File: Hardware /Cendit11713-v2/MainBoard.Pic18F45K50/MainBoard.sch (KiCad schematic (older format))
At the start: 32 parts, among them CON1 VIKING_BOARD_CON, CON2 USB_CON, J1 RESET_CON, U1 PIC18F45K50-X/PT, U2 SER_BUS_ADDR_CON

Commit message: Respaldo rapido
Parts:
- CON2: symbol USB_CON -> USB_CON-RESCUE-MainBoard
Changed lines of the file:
@@
 EESchema Schematic File Version 2
+LIBS:MainBoard-rescue
 LIBS:adc-dac
 LIBS:memory
@@
 $EndComp
 $Comp
-L POWER_CON #CON01
+L POWER_CON-RESCUE-MainBoard #CON01
 U 1 1 5996E2AE
 P 1000 2000
@@
 $EndComp
 $Comp
-L USB_CON CON2
+L USB_CON-RESCUE-MainBoard CON2
 U 1 1 5996E56B
 P 1000 3000

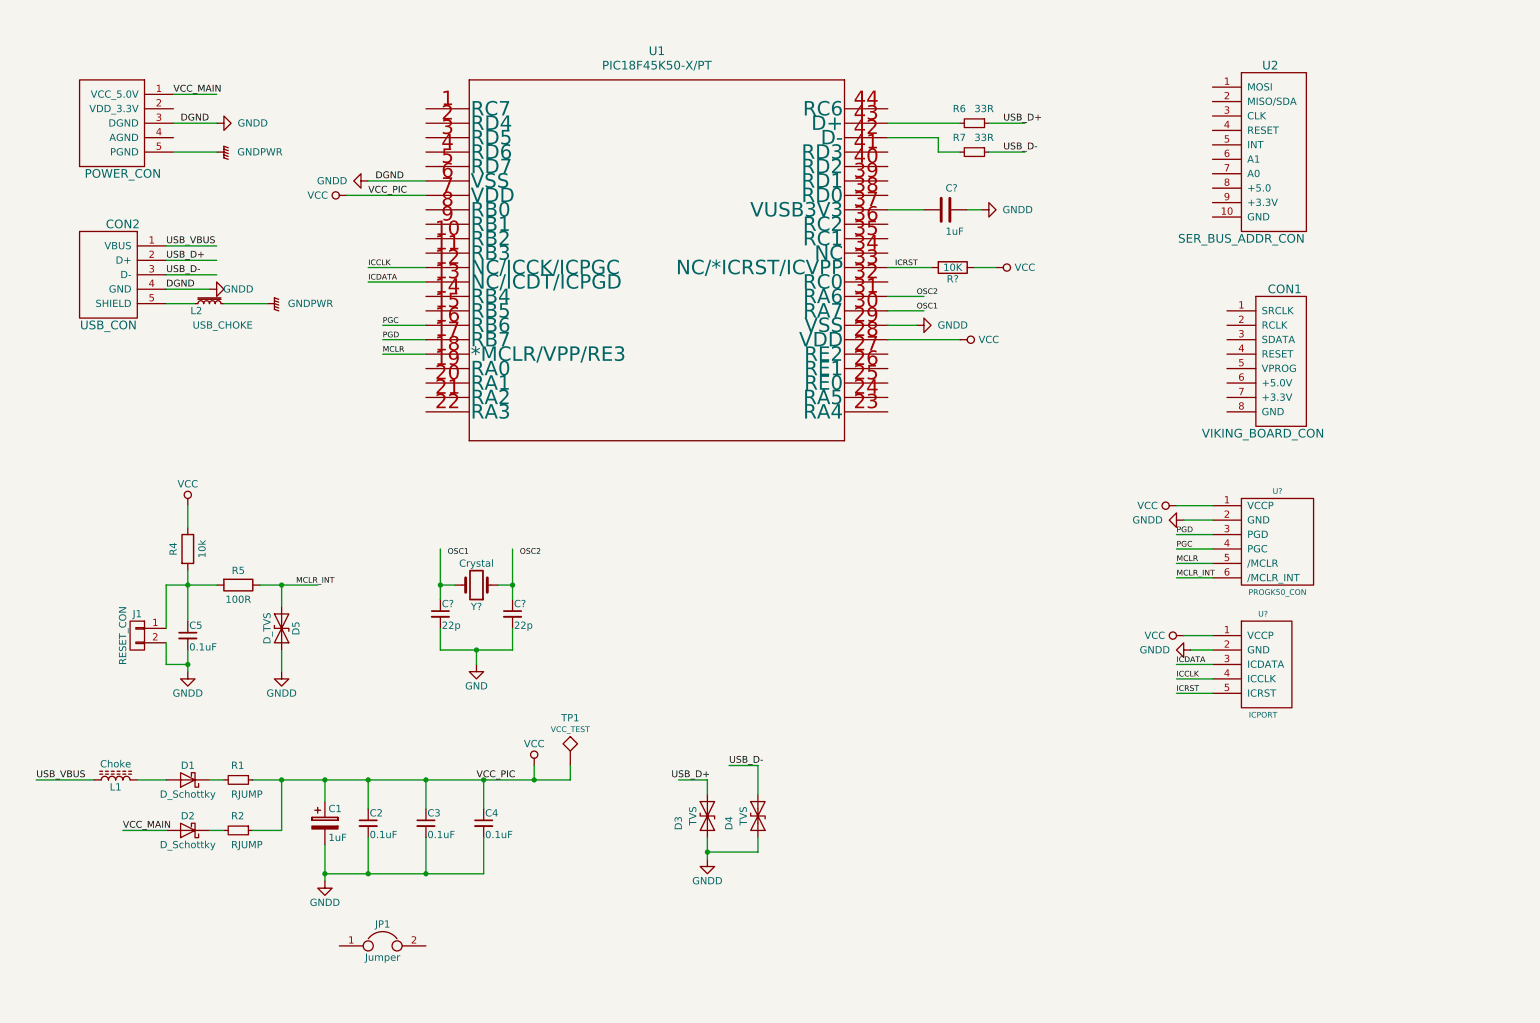
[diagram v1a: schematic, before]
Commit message: En Cendit11713 + respaldo de software
  - Esquematico tarjeta madre con PIC18F45K50
  - Respaldo de software CenditLab
  - Gerber files tarjeta interfaz GPIB
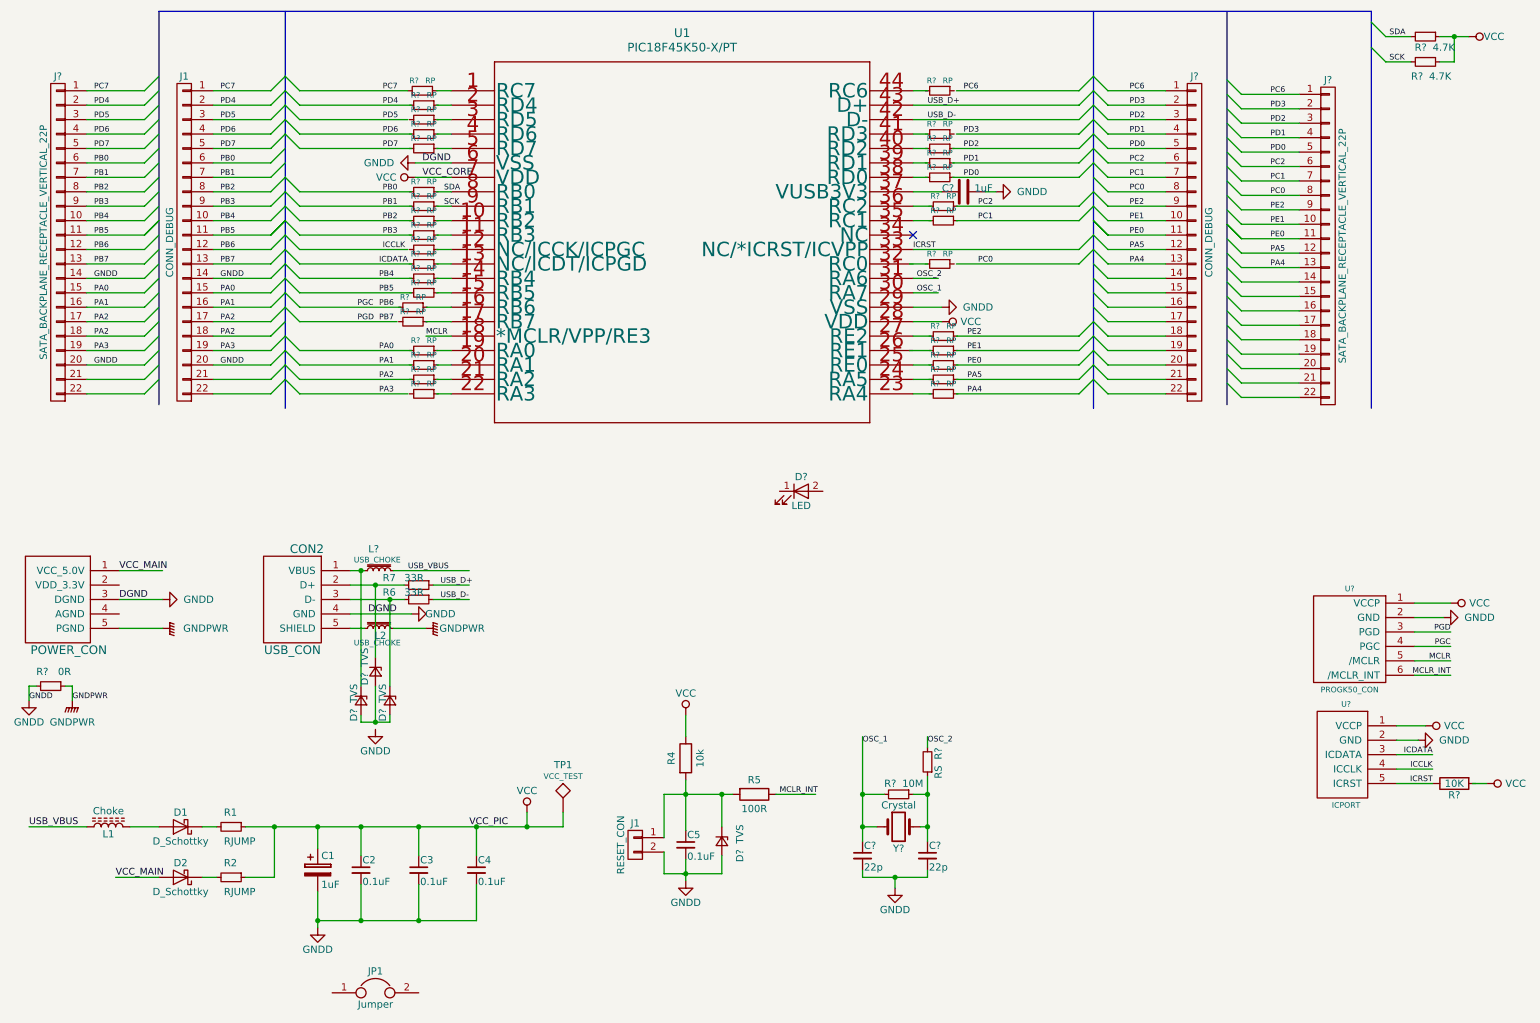
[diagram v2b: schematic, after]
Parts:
- removed C? (x2): 22p, symbol C_Small
- removed CON1: VIKING_BOARD_CON, symbol VIKING_BOARD_CON
- removed D3, D4: TVS, symbol D_TVS
- removed D5: D_TVS, symbol D_TVS
- removed U2: SER_BUS_ADDR_CON, symbol SER_BUS_ADDR_CON
- removed Y?: Crystal, symbol Crystal
- added C? (x2): 22p, symbol C_Small
- added D? (x4): TVS, symbol D_Zener_Small
- added D?: LED, symbol LED
- added J1, J?: CONN_DEBUG, symbol CONN_01X22
- added J? (x2): SATA_BACKPLANE_RECEPTACLE_VERTICAL_22P, symbol CONN_01X22
- added L?: USB_CHOKE, symbol L_Core_Iron_Small
- added R?: 0R, symbol R_Small
- added R? (x32): RP, symbol R_Small
- added R?: 10M, symbol R_Small
- added R?: RS, symbol R_Small
- added R? (x2): 4.7K, symbol R_Small
- added Y?: Crystal, symbol Crystal
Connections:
- net labels added: OSC_1, OSC_2, PA0, PA1, PA2, PA3, PA4, PA5, PB0, PB1, PB2, PB3, PB4, PB5, PB6, PB7, PC0, PC1, PC2, PC6, PC7, PD0, PD1, PD2, PD3, PD4, PD5, PD6, PD7, PE0, PE1, PE2, SCK, SDA, VCC_CORE
- net labels removed: GND, OSC1, OSC2
- wire segments 85 -> 245
- no-connect marks 0 -> 1
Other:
- moved on the sheet: C1, C2, C3, C4, C5, C?, CON2, D1, D2, J1, JP1, L1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
